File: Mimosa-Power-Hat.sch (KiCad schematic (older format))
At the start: 74 parts, among them J1 Screw_Terminal_01x04, J2 Screw_Terminal_01x02, J3 40HAT, J4 Screw_Terminal_01x02, J5 Screw_Terminal_01x04, J9 CONN_01X02, M1 Fan_Tacho_PWM, Q1 DMG2305UX, Q2 DMMT5401, U1 ADM3490ExR, U2 CAT24C32, U3 TCAN330, U4 LMZ13608, U5 AB0805, U6 MCP2515-xSO, U7 TXB0102DCU, Y1 32.768 kHz, Y2 8MHz

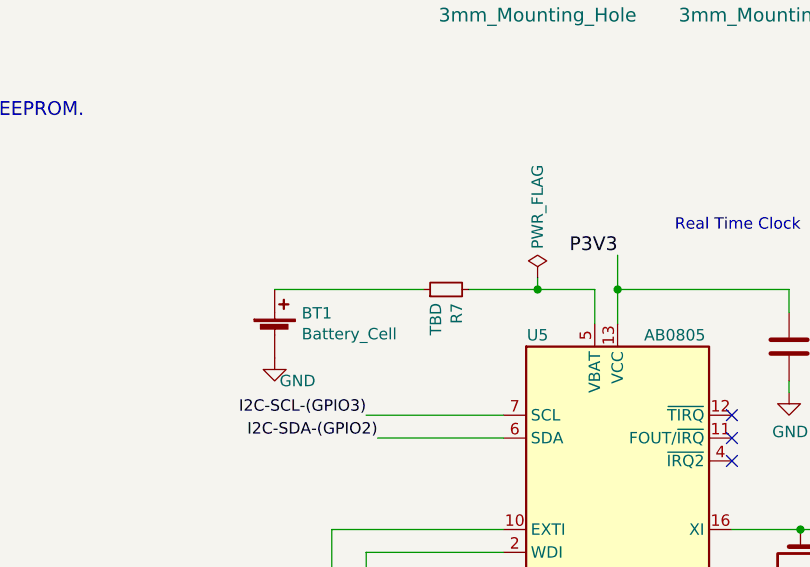
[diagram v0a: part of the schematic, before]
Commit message: Assembly documents
adding Assembly files
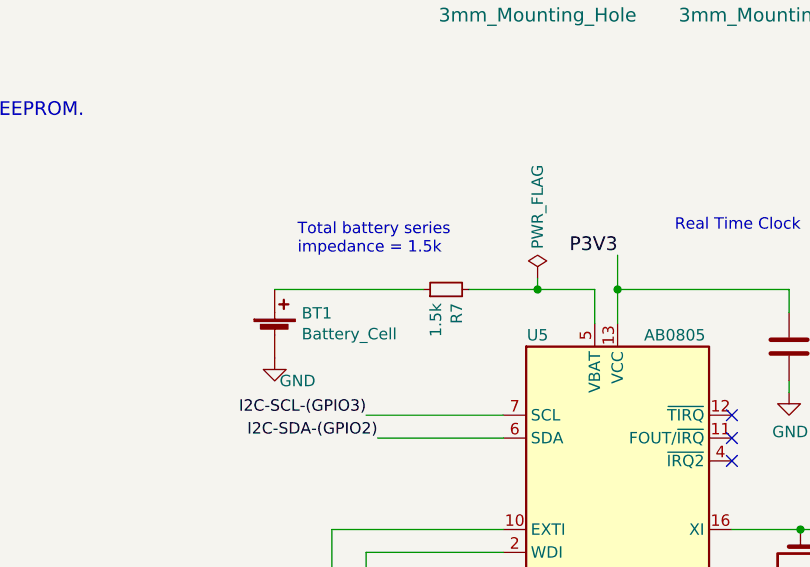
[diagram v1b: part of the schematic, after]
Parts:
- R7: value TBD -> 1.5k
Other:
- note added: "Total battery series\nimpedance = 1.5k"
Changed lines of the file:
@@
 P 5250 7900
 F 0 "R7" H 5191 7854 50  0000 R CNN
-F 1 "TBD" H 5191 7945 50  0000 R CNN
+F 1 "1.5k" H 5191 7945 50  0000 R CNN
 F 2 "Resistor_SMD:R_0805_2012Metric_Pad1.15x1.40mm_HandSolder" H 5250 7900 50  0001 C CNN
 F 3 "~" H 5250 7900 50  0001 C CNN
@@
 $EndComp
 Connection ~ 14250 950
+Text Notes 4600 7750 0    50   ~ 0
+Total battery series\nimpedance = 1.5k
 $EndSCHEMATC

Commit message: Creation of V1 - correction 1
- Correction of battery holder who was not the proper size
- Changed 12 to 5 DC regulator for a much cheaper one.
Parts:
- removed C1: 150uF, Capacitor_SMD:CP_Elec_10x12.5, symbol Device:CP
- removed C10: 470nF, Capacitor_SMD:C_0805_2012Metric_Pad1.15x1.40mm_HandSolder, symbol Device:C
- removed C14, C15: 330uF, Capacitor_Tantalum_SMD:CP_EIA-7343-31_Kemet-D_Pad2.25x2.55mm_HandSolder, symbol Device:C
- removed C16: 47uF, Capacitor_SMD:C_0805_2012Metric_Pad1.15x1.40mm_HandSolder, symbol Device:C
- removed C17, C18, C6, C9: 47nF, Capacitor_SMD:C_0805_2012Metric_Pad1.15x1.40mm_HandSolder, symbol Device:C
- removed C2, C3, C4: 10uF, Capacitor_SMD:C_0805_2012Metric_Pad1.15x1.40mm_HandSolder, symbol Device:C
- removed R14: 8k, Resistor_SMD:R_0805_2012Metric_Pad1.15x1.40mm_HandSolder, symbol Device:R
- removed R15: 1.5k, Resistor_SMD:R_0805_2012Metric_Pad1.15x1.40mm_HandSolder, symbol Device:R
- removed U4: LMZ13608, Package_TO_SOT_SMD:Texas_NDY0011A, symbol Regulator_Switching:LMZ13608
- added C28, C29, C30, C31: 10uF, Capacitor_Tantalum_SMD:CP_EIA-7343-31_Kemet-D, symbol Device:C_Polarized
- added C32: 470nF, Capacitor_SMD:C_0805_2012Metric, symbol Device:C
- added C33: 10nF, Capacitor_SMD:C_0805_2012Metric, symbol Device:C
- added C34, C35, C36: 150uF, Capacitor_Tantalum_SMD:CP_EIA-7343-31_Kemet-D, symbol Device:C_Polarized
- added D2: 6TQ045S, Package_TO_SOT_SMD:TO-263-2, symbol Device:D_Schottky_AKA
- added L1: 15uH, Inductor_SMD:L_11.5x10.3_H4mm, symbol Device:L
- added U8: LM2678, Package_TO_SOT_SMD:TO-263-7_TabPin4, symbol Regulator_Switching:LM2678
- BT1: footprint Battery:BatteryHolder_Keystone_2998_1x6.8mm -> Battery:BatteryHolder_Keystone_3000_1x12mm
- D1: symbol Device:D_TVS_x2_AAC -> Mimosa-Power-Hat-rescue:D_TVS_x2_AAC-Device
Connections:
- wire segments 295 -> 280
- no-connect marks 29 -> 30
